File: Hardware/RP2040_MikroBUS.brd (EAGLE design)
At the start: 30.5 x 94 mm, 162 parts, among them J1 SWD, J3 Qwiic, J5 USB C, J6 microSD, J9 MIKROBUS_SMD_BLACK1, Q1 20V/4.2A/52mΩ/1.4W, U2 MAX17048, U3 MCP73831, U4 W25QXX128MBIT, U5 RP2040, U7 3.3V, Y2 12MHz

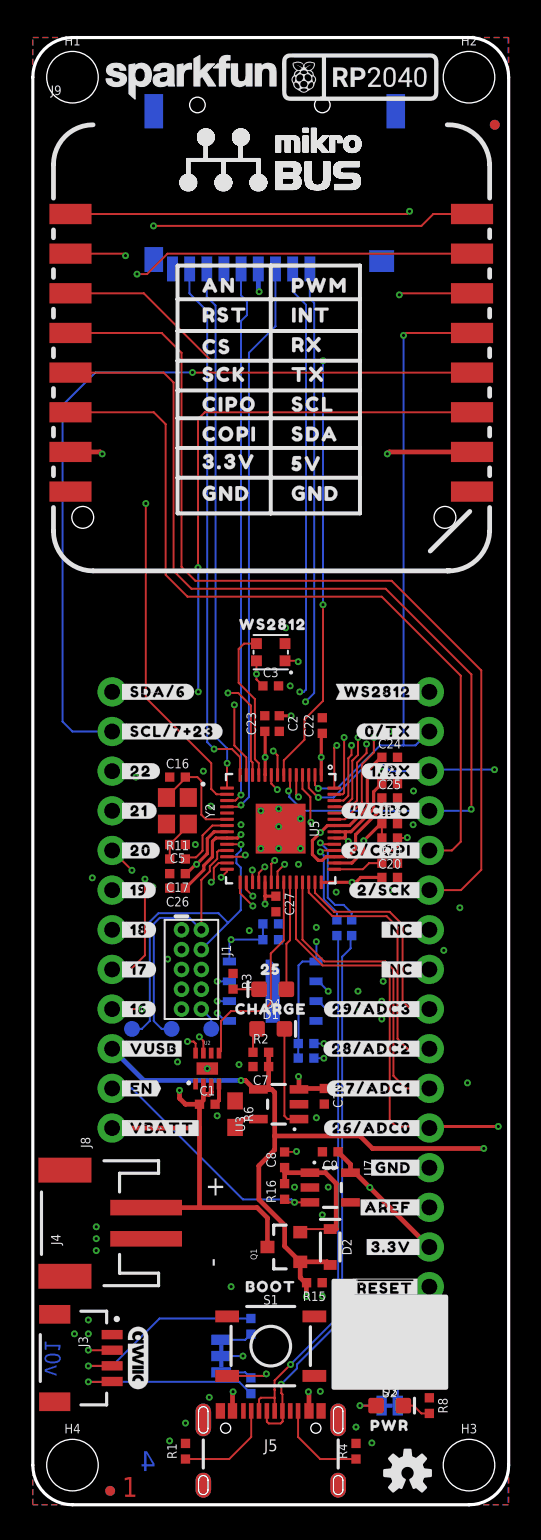
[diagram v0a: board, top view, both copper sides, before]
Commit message: Design review updates
* Bump version number
* Remove CS_PU label from borrom
* Move SWDCK TP
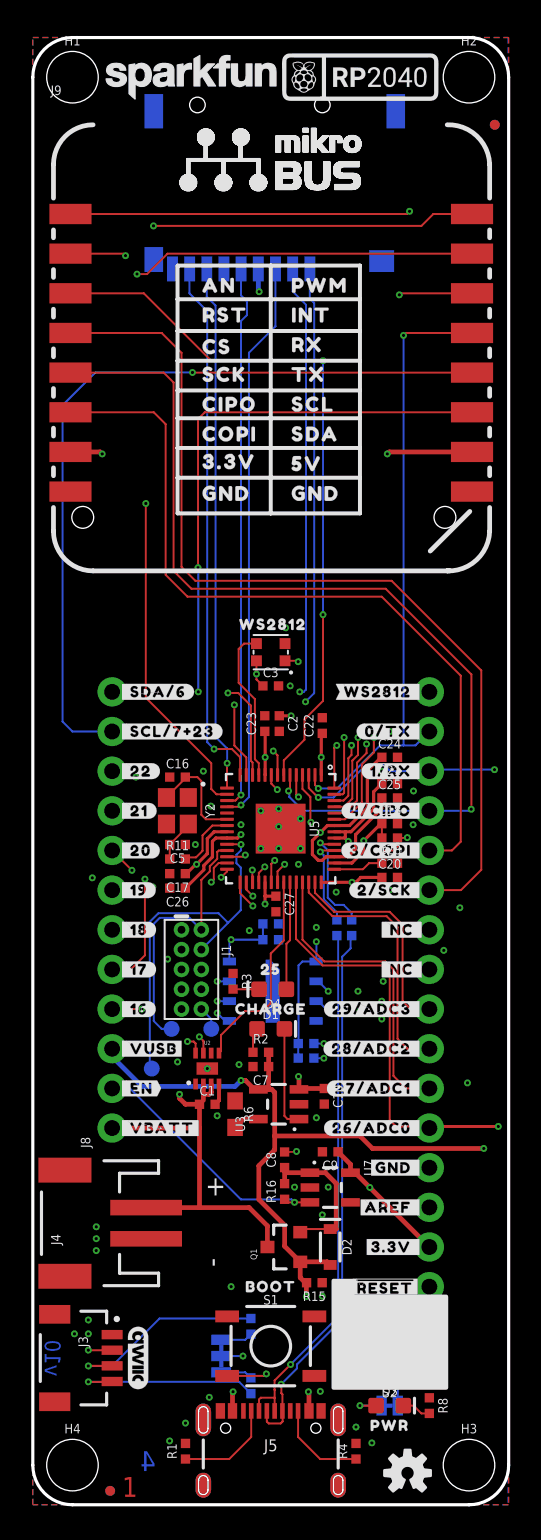
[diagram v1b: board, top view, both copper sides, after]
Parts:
- removed U$86: (no value), output:#CS_PU#0
- moved TP1 2.84 mm to (7.62, 27.9)
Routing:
- net SWDCK: track 22.1 -> 23.9 mm
- net V_USB: track 110.7 -> 111.3 mm
- net !BATT_ALERT!: track 13.8 -> 13.3 mm
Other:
- board text added: "v10"
- board text removed: "v01"
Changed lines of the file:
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@@
 <drawing>
 <settings>
-<setting alwaysvectorfont="no"/>
+<setting alwaysvectorfont="yes"/>
 <setting keepoldvectorfont="yes"/>
 <setting verticaltext="up"/>
@@
 <layer number="45" name="Holes" color="7" fill="1" visible="yes" active="yes"/>
 <layer number="46" name="Milling" color="3" fill="1" visible="no" active="yes"/>
-<layer number="47" name="Measures" color="7" fill="1" visible="no" active="yes"/>
+<layer number="47" name="Measures" color="7" fill="1" visible="yes" active="yes"/>
 <layer number="48" name="Document" color="7" fill="1" visible="no" active="yes"/>
 <layer number="49" name="Reference" color="7" fill="1" visible="no" active="yes"/>
@@
 <layer number="95" name="Names" color="7" fill="1" visible="no" active="no"/>
 <layer number="96" name="Values" color="7" fill="1" visible="no" active="no"/>
-<layer number="2" name="gndvert" color="10" fill="7" visible="yes" active="yes"/>
-<layer number="15" name="pwrhorz" color="4" fill="7" visible="yes" active="yes"/>
+<layer number="2" name="gndvert" color="10" fill="7" visible="no" active="yes"/>
+<layer number="15" name="pwrhorz" color="4" fill="7" visible="no" active="yes"/>
 <layer number="3" name="Route3" color="4" fill="3" visible="no" active="no"/>
 <layer number="4" name="Route4" color="1" fill="4" visible="no" active="no"/>
@@
 <wire x1="2.54" y1="0" x2="0" y2="2.54" width="0.2032" layer="20" curve="-90"/>
 <wire x1="0" y1="2.54" x2="0" y2="91.44" width="0.2032" layer="20"/>
-<text x="1.27" y="9.398" size="1.016" layer="16" font="vector" ratio="20" rot="MR90" align="center">v01</text>
+<text x="1.27" y="9.398" size="1.016" layer="16" font="vector" ratio="20" rot="MR90" align="center">v10</text>
 <dimension x1="0" y1="0" x2="2.286" y2="18.415" x3="-8.763" y3="9.2075" textsize="1.27" textratio="15" layer="47" dtype="vertical" unit="inch"/>
 <dimension x1="0" y1="0" x2="2.54" y2="2.54" x3="1.27" y3="-10.16" textsize="1.27" textratio="15" layer="47" dtype="horizontal" unit="inch"/>
@@
 <wire x1="30.48" y1="91.44" x2="27.94" y2="93.98" width="0.2032" layer="20" curve="90"/>
 <dimension x1="0" y1="0" x2="30.48" y2="0" x3="15.24" y3="-11.43" textsize="1.778" textratio="15" layer="47" unit="inch"/>
-<dimension x1="4.445" y1="56.388" x2="4.445" y2="0" x3="-11.43" y3="28.194" textsize="1.778" textratio="15" layer="47" unit="inch"/>
 <dimension x1="0" y1="0" x2="0" y2="93.98" x3="-15.24" y3="46.99" textsize="1.778" textratio="15" layer="47" unit="inch"/>
 <dimension x1="0" y1="0" x2="27.94" y2="0" x3="13.97" y3="-7.62" textsize="1.778" textratio="15" layer="47" unit="inch"/>
@@
 </element>
 <element name="U$16" library="output" package="PWR0" value="" x="22.86" y="5.08" smashed="yes"/>
-<element name="TP1" library="SparkFun-Connectors" package="PAD.03X.04" value="TEST-POINT3X4" x="6.35" y="30.48" smashed="yes" rot="MR0"/>
+<element name="TP1" library="SparkFun-Connectors" package="PAD.03X.04" value="TEST-POINT3X4" x="7.62" y="27.94" smashed="yes" rot="MR0"/>
 <element name="TP2" library="SparkFun-Connectors" package="PAD.03X.04" value="TEST-POINT3X4" x="8.89" y="30.48" smashed="yes" rot="MR0"/>
 <element name="TP3" library="SparkFun-Connectors" package="PAD.03X.04" value="TEST-POINT3X4" x="11.43" y="30.48" smashed="yes" rot="MR0"/>
@@
 <attribute name="VALUE" x="22.86" y="7.493" size="0.6096" layer="28" font="vector" ratio="20" rot="MR180" align="top-center"/>
 </element>
-<element name="U$86" library="output" package="#CS_PU#0" value="" x="18.161" y="63.5" smashed="yes" rot="MR0"/>
 <element name="U$87" library="output" package="#PWR#0" value="" x="28.448" y="6.35" smashed="yes" rot="MR0"/>
 <element name="U$88" library="output" package="MIKROBUS0" value="" x="22.352" y="67.056" smashed="yes" rot="MR0"/>
@@
 <wire x1="13.6199" y1="27.178" x2="13.335" y2="27.178" width="0.3048" layer="1"/>
 <via x="13.335" y="27.178" extent="1-16" drill="0.2" diameter="0.45"/>
-<wire x1="13.335" y1="27.178" x2="7.112" y2="27.178" width="0.3048" layer="16"/>
-<wire x1="7.112" y1="27.178" x2="5.08" y2="29.21" width="0.3048" layer="16"/>
+<wire x1="13.335" y1="27.178" x2="12.954" y2="26.797" width="0.3048" layer="16"/>
+<wire x1="12.954" y1="26.797" x2="6.985" y2="26.797" width="0.3048" layer="16"/>
+<wire x1="6.985" y1="26.797" x2="5.08" y2="28.702" width="0.3048" layer="16"/>
+<wire x1="5.08" y1="28.702" x2="5.08" y2="29.21" width="0.3048" layer="16"/>
 <wire x1="17.69" y1="6.01" x2="17.69" y2="7.202" width="0.3048" layer="1"/>
 <wire x1="17.69" y1="7.202" x2="17.653" y2="7.239" width="0.254" layer="1"/>
@@
 <wire x1="10.676" y1="24.13" x2="10.676" y2="25.654" width="0.127" layer="1"/>
 <wire x1="7.256" y1="19.034" x2="10.668" y2="19.034" width="0.3048" layer="1"/>
-<wire x1="10.668" y1="19.034" x2="14.367" y2="19.034" width="0.3048" layer="1"/>
-<wire x1="15.029" y1="18.372" x2="15.029" y2="16.51" width="0.3048" layer="1"/>
-<wire x1="14.367" y1="19.034" x2="15.029" y2="18.372" width="0.3048" layer="1"/>
+<wire x1="10.668" y1="19.034" x2="13.859" y2="19.034" width="0.3048" layer="1"/>
+<wire x1="15.029" y1="17.864" x2="15.029" y2="16.51" width="0.3048" layer="1"/>
+<wire x1="13.859" y1="19.034" x2="15.029" y2="17.864" width="0.3048" layer="1"/>
 <wire x1="17.0481" y1="26.604" x2="17.1061" y2="26.662" width="0.254" layer="1"/>
 <wire x1="17.1061" y1="26.662" x2="18.669" y2="26.662" width="0.3048" layer="1"/>
@@
 <wire x1="17.018" y1="27.432" x2="16.764" y2="27.686" width="0.3048" layer="15"/>
 <wire x1="16.764" y1="27.686" x2="12.052" y2="27.686" width="0.3048" layer="15"/>
-<wire x1="9.398" y1="26.543" x2="10.909" y2="26.543" width="0.3048" layer="15"/>
-<wire x1="12.052" y1="27.686" x2="10.909" y2="26.543" width="0.3048" layer="15"/>
-<via x="9.398" y="26.543" extent="1-16" drill="0.2" diameter="0.45"/>
-<wire x1="9.398" y1="26.543" x2="9.398" y2="26.035" width="0.3048" layer="1"/>
+<wire x1="9.398" y1="26.289" x2="10.655" y2="26.289" width="0.3048" layer="15"/>
+<wire x1="12.052" y1="27.686" x2="10.655" y2="26.289" width="0.3048" layer="15"/>
+<via x="9.398" y="26.289" extent="1-16" drill="0.2" diameter="0.45"/>
+<wire x1="9.398" y1="26.289" x2="9.398" y2="26.035" width="0.3048" layer="1"/>
 <wire x1="9.779" y1="25.654" x2="9.398" y2="26.035" width="0.3048" layer="1"/>
 <wire x1="9.779" y1="25.654" x2="10.676" y2="25.654" width="0.3048" layer="1"/>
@@
 <wire x1="16.764" y1="19.37" x2="16.325" y2="19.37" width="0.127" layer="1"/>
 <wire x1="16.325" y1="19.37" x2="16.129" y2="19.566" width="0.127" layer="1"/>
-<wire x1="6.35" y1="26.67" x2="13.462" y2="19.558" width="0.127" layer="16"/>
-<wire x1="6.35" y1="26.67" x2="5.08" y2="26.67" width="0.127" layer="16"/>
+<wire x1="6.223" y1="26.67" x2="13.335" y2="19.558" width="0.127" layer="16"/>
+<wire x1="6.223" y1="26.67" x2="5.08" y2="26.67" width="0.127" layer="16"/>
 <wire x1="16.576" y1="19.558" x2="16.764" y2="19.37" width="0.127" layer="16"/>
 <via x="16.764" y="19.37" extent="1-16" drill="0.2" diameter="0.45"/>
-<wire x1="13.462" y1="19.558" x2="16.576" y2="19.558" width="0.127" layer="16"/>
+<wire x1="13.335" y1="19.558" x2="16.576" y2="19.558" width="0.127" layer="16"/>
 </signal>
 <signal name="N$2">
@@
 <wire x1="13.3225" y1="38.0875" x2="12.5095" y2="37.2745" width="0.127" layer="16"/>
 <wire x1="12.5095" y1="37.2745" x2="10.795" y2="35.56" width="0.127" layer="16"/>
-<wire x1="7.493" y1="37.338" x2="7.493" y2="30.988" width="0.127" layer="16"/>
-<wire x1="7.493" y1="30.988" x2="6.985" y2="30.48" width="0.127" layer="16"/>
-<wire x1="6.35" y1="30.48" x2="6.985" y2="30.48" width="0.127" layer="16"/>
+<wire x1="7.62" y1="27.94" x2="7.493" y2="28.067" width="0.127" layer="16"/>
+<wire x1="7.493" y1="37.338" x2="7.493" y2="28.067" width="0.127" layer="16"/>
 <wire x1="7.493" y1="37.338" x2="8.0439" y2="37.8889" width="0.127" layer="16"/>
 <wire x1="11.8951" y1="37.8889" x2="12.5095" y2="37.2745" width="0.127" layer="16"/>
@@
 <wire x1="15.24" y1="35.306" x2="15.24" y2="32.131" width="0.127" layer="1"/>
 <wire x1="15.24" y1="32.131" x2="14.732" y2="31.623" width="0.127" layer="1"/>
-<wire x1="14.732" y1="31.623" x2="12.7" y2="31.623" width="0.127" layer="1"/>
-<wire x1="12.7" y1="31.623" x2="12.053" y2="30.976" width="0.127" layer="1"/>
-<wire x1="12.053" y1="30.976" x2="12.053" y2="29.057" width="0.127" layer="1"/>
+<wire x1="14.732" y1="31.623" x2="13.589" y2="31.623" width="0.127" layer="1"/>
+<wire x1="13.589" y1="31.623" x2="12.053" y2="30.087" width="0.127" layer="1"/>
+<wire x1="12.053" y1="30.087" x2="12.053" y2="29.057" width="0.127" layer="1"/>
 <wire x1="12.053" y1="29.057" x2="11.926" y2="28.93" width="0.127" layer="1"/>
 </signal>
@@
 <contactref element="J9" pad="3"/>
 <wire x1="16.075" y1="46.7435" x2="16.075" y2="47.675" width="0.127" layer="1"/>
-<via x="18.588" y="57.6489" extent="1-16" drill="0.2" diameter="0.45"/>
+<via x="18.588" y="57.0139" extent="1-16" drill="0.2" diameter="0.45"/>
 <via x="18.588" y="73.279" extent="1-16" drill="0.2" diameter="0.45"/>
 <wire x1="18.588" y1="73.279" x2="11.43" y2="73.279" width="0.127" layer="1"/>
@@
 <wire x1="7.112" y1="77.597" x2="2.413" y2="77.597" width="0.127" layer="1"/>
 <wire x1="18.588" y1="51.488" x2="17.4" y2="50.3" width="0.127" layer="1"/>
-<wire x1="18.588" y1="57.6489" x2="18.588" y2="51.488" width="0.127" layer="1"/>
+<wire x1="18.588" y1="57.0139" x2="18.588" y2="51.488" width="0.127" layer="1"/>
 <wire x1="17.4" y1="50.3" x2="17.4" y2="49" width="0.127" layer="1"/>
 <wire x1="17.4" y1="49" x2="16.075" y2="47.675" width="0.127" layer="1"/>
-<wire x1="18.588" y1="57.6489" x2="18.588" y2="73.279" width="0.127" layer="16"/>
+<wire x1="18.588" y1="57.0139" x2="18.588" y2="73.279" width="0.127" layer="16"/>
 </signal>
 <signal name="N$10">

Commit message: Update RP2040_MikroBUS.brd
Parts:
- removed U$87: (no value), output:#PWR#0
- added U$43: (no value), output:#LED#0
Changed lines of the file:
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@@
 <?xml version="1.0" encoding="utf-8"?>
 <!DOCTYPE eagle SYSTEM "eagle.dtd">
-<eagle version="9.5.2">
+<eagle version="9.6.2">
 <drawing>
 <settings>
-<setting alwaysvectorfont="yes"/>
+<setting alwaysvectorfont="no"/>
 <setting keepoldvectorfont="yes"/>
 <setting verticaltext="up"/>
@@
 <attribute name="VALUE" x="22.86" y="7.493" size="0.6096" layer="28" font="vector" ratio="20" rot="MR180" align="top-center"/>
 </element>
-<element name="U$87" library="output" package="#PWR#0" value="" x="28.448" y="6.35" smashed="yes" rot="MR0"/>
 <element name="U$88" library="output" package="MIKROBUS0" value="" x="22.352" y="67.056" smashed="yes" rot="MR0"/>
+<element name="U$43" library="output" package="#LED#0" value="" x="27.94" y="6.35" smashed="yes" rot="MR0"/>
 </elements>
 <signals>

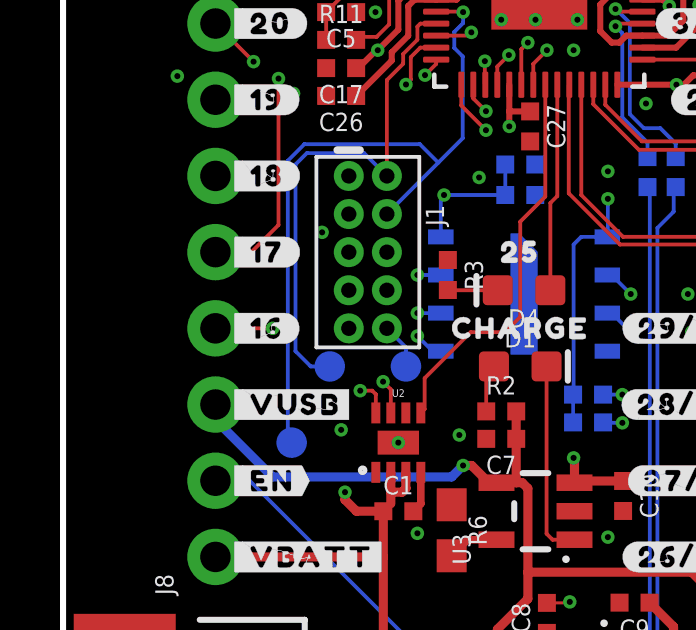
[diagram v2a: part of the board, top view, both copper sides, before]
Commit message: QC Double check
* Added label for PWR jumper
* Moved GPIO16 via
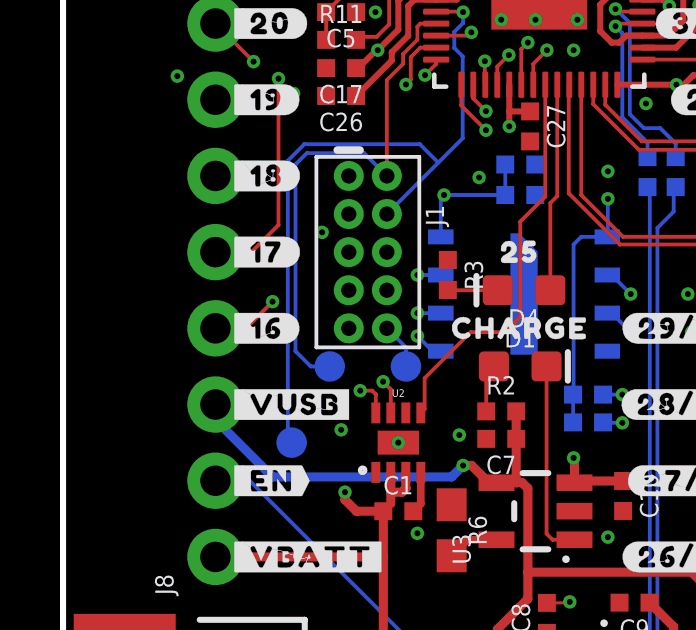
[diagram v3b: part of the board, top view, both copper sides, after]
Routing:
- net GPIO16: track 79.0 -> 78.5 mm
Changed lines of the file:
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@@
 <?xml version="1.0" encoding="utf-8"?>
 <!DOCTYPE eagle SYSTEM "eagle.dtd">
-<eagle version="9.6.2">
+<eagle version="9.5.2">
 <drawing>
 <settings>
@@
 <layer number="45" name="Holes" color="7" fill="1" visible="yes" active="yes"/>
 <layer number="46" name="Milling" color="3" fill="1" visible="no" active="yes"/>
-<layer number="47" name="Measures" color="7" fill="1" visible="yes" active="yes"/>
+<layer number="47" name="Measures" color="7" fill="1" visible="no" active="yes"/>
 <layer number="48" name="Document" color="7" fill="1" visible="no" active="yes"/>
 <layer number="49" name="Reference" color="7" fill="1" visible="no" active="yes"/>
@@
 <layer number="95" name="Names" color="7" fill="1" visible="no" active="no"/>
 <layer number="96" name="Values" color="7" fill="1" visible="no" active="no"/>
-<layer number="2" name="gndvert" color="10" fill="7" visible="no" active="yes"/>
-<layer number="15" name="pwrhorz" color="4" fill="7" visible="no" active="yes"/>
+<layer number="2" name="gndvert" color="10" fill="7" visible="yes" active="yes"/>
+<layer number="15" name="pwrhorz" color="4" fill="7" visible="yes" active="yes"/>
 <layer number="3" name="Route3" color="4" fill="3" visible="no" active="no"/>
 <layer number="4" name="Route4" color="1" fill="4" visible="no" active="no"/>
@@
 <wire x1="11.5915" y1="40.7906625" x2="11.5915" y2="40.0395" width="0.127" layer="1"/>
 <wire x1="11.5915" y1="40.0395" x2="11.43" y2="39.878" width="0.127" layer="1"/>
-<via x="6.985" y="31.75" extent="1-16" drill="0.2" diameter="0.45"/>
-<wire x1="6.985" y1="31.75" x2="5.08" y2="31.75" width="0.127" layer="1"/>
+<via x="6.985" y="32.639" extent="1-16" drill="0.2" diameter="0.45"/>
+<wire x1="6.985" y1="32.639" x2="6.096" y2="31.75" width="0.127" layer="1"/>
+<wire x1="6.096" y1="31.75" x2="5.08" y2="31.75" width="0.127" layer="1"/>
 <contactref element="J9" pad="16"/>
 <wire x1="28.133" y1="82.677" x2="25.654" y2="82.677" width="0.127" layer="1"/>
@@
 <wire x1="7.858" y1="81.788" x2="7.858" y2="39.751" width="0.127" layer="2"/>
 <wire x1="7.858" y1="39.751" x2="7.685" y2="39.578" width="0.127" layer="2"/>
-<wire x1="7.685" y1="39.578" x2="7.685" y2="32.45" width="0.127" layer="2"/>
-<wire x1="7.685" y1="32.45" x2="6.985" y2="31.75" width="0.127" layer="2"/>
+<wire x1="7.685" y1="39.578" x2="7.685" y2="33.339" width="0.127" layer="2"/>
+<wire x1="7.685" y1="33.339" x2="6.985" y2="32.639" width="0.127" layer="2"/>
 <wire x1="11.43" y1="39.878" x2="11.13" y2="39.578" width="0.127" layer="15"/>
 <wire x1="11.13" y1="39.578" x2="7.685" y2="39.578" width="0.127" layer="15"/>
